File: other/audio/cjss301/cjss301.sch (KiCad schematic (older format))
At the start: 81 parts, among them J50 DC 12V in, J51 PHONO, J52 RADIO, J53 TAPE, J54 SPEAKERS, Q1 BC559C, Q2 BC549C, Q21 BC559C, Q22 BC549C, Q23 BC549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

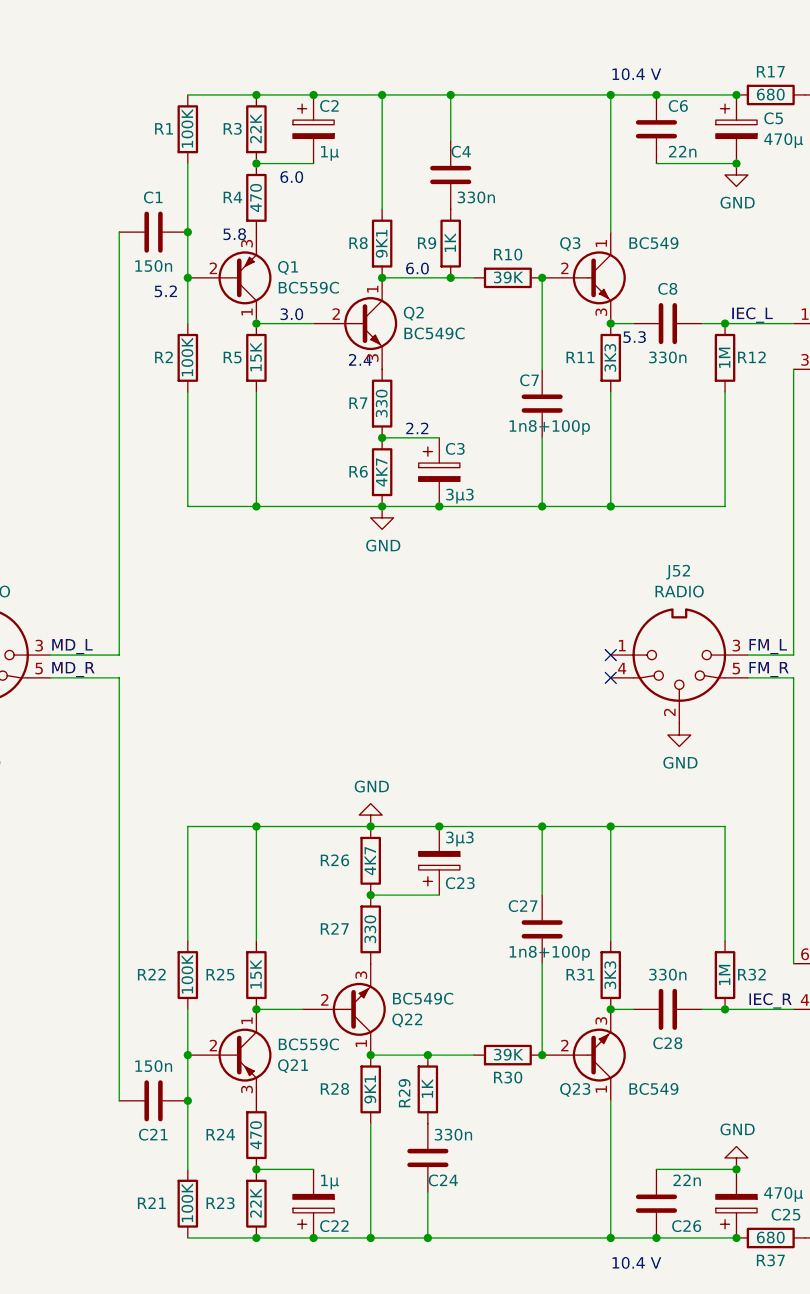
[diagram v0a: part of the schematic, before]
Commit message: correct decoupling capacitors
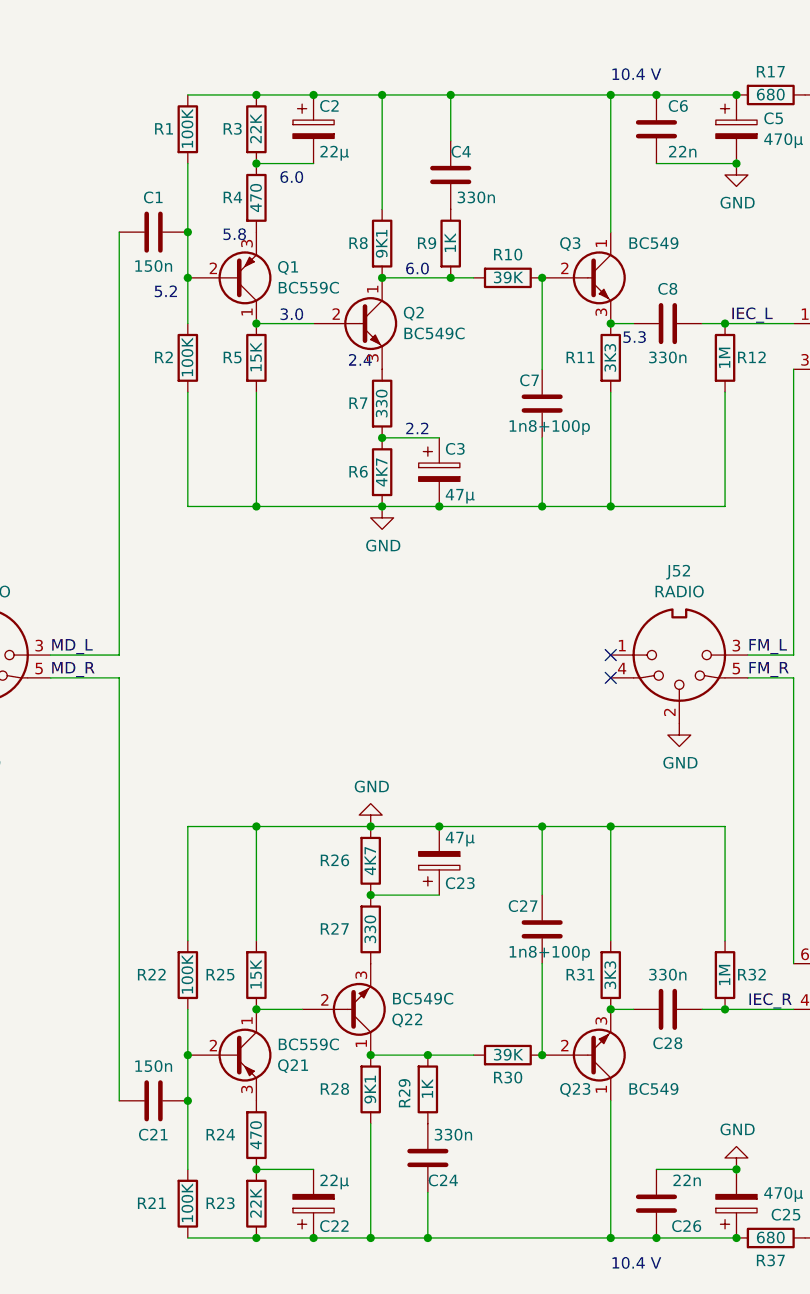
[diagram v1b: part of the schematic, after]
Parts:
- C2, C22: value 1µ -> 22µ
- C23, C3: value 3µ3 -> 47µ
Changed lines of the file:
@@
 P 2950 1000
 F 0 "C2" H 2975 1100 50  0000 L CNN
-F 1 "1µ" H 2975 900 50  0000 L CNN
+F 1 "22µ" H 2975 900 50  0000 L CNN
 F 2 "Capacitor_THT:CP_Radial_D4.0mm_P2.00mm" H 2988 850 50  0001 C CNN
 F 3 "~" H 2950 1000 50  0001 C CNN
@@
 P 3500 2500
 F 0 "C3" H 3525 2600 50  0000 L CNN
-F 1 "3µ3" H 3525 2400 50  0000 L CNN
+F 1 "47µ" H 3525 2400 50  0000 L CNN
 F 2 "Capacitor_THT:CP_Radial_D5.0mm_P2.00mm" H 3538 2350 50  0001 C CNN
 F 3 "~" H 3500 2500 50  0001 C CNN
@@
 P 2950 5700
 F 0 "C22" H 2975 5800 50  0000 L CNN
-F 1 "1µ" H 2975 5600 50  0000 L CNN
+F 1 "22µ" H 2975 5600 50  0000 L CNN
 F 2 "Capacitor_THT:CP_Radial_D4.0mm_P2.00mm" H 2988 5550 50  0001 C CNN
 F 3 "~" H 2950 5700 50  0001 C CNN
@@
 P 3500 4200
 F 0 "C23" H 3525 4300 50  0000 L CNN
-F 1 "3µ3" H 3525 4100 50  0000 L CNN
+F 1 "47µ" H 3525 4100 50  0000 L CNN
 F 2 "Capacitor_THT:CP_Radial_D5.0mm_P2.00mm" H 3538 4050 50  0001 C CNN
 F 3 "~" H 3500 4200 50  0001 C CNN
